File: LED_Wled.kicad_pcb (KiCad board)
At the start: 2 copper layers, 67 x 27 mm, 25 parts, among them J1 SWD_PORT_SKEDD, Q1 BSS138, Q2 AO4485, Q3 BSS138, Q4 AO4485, U1 ESP8266-12E_ESP-12E, U2 XL1509, U3 LD1117DT33TR

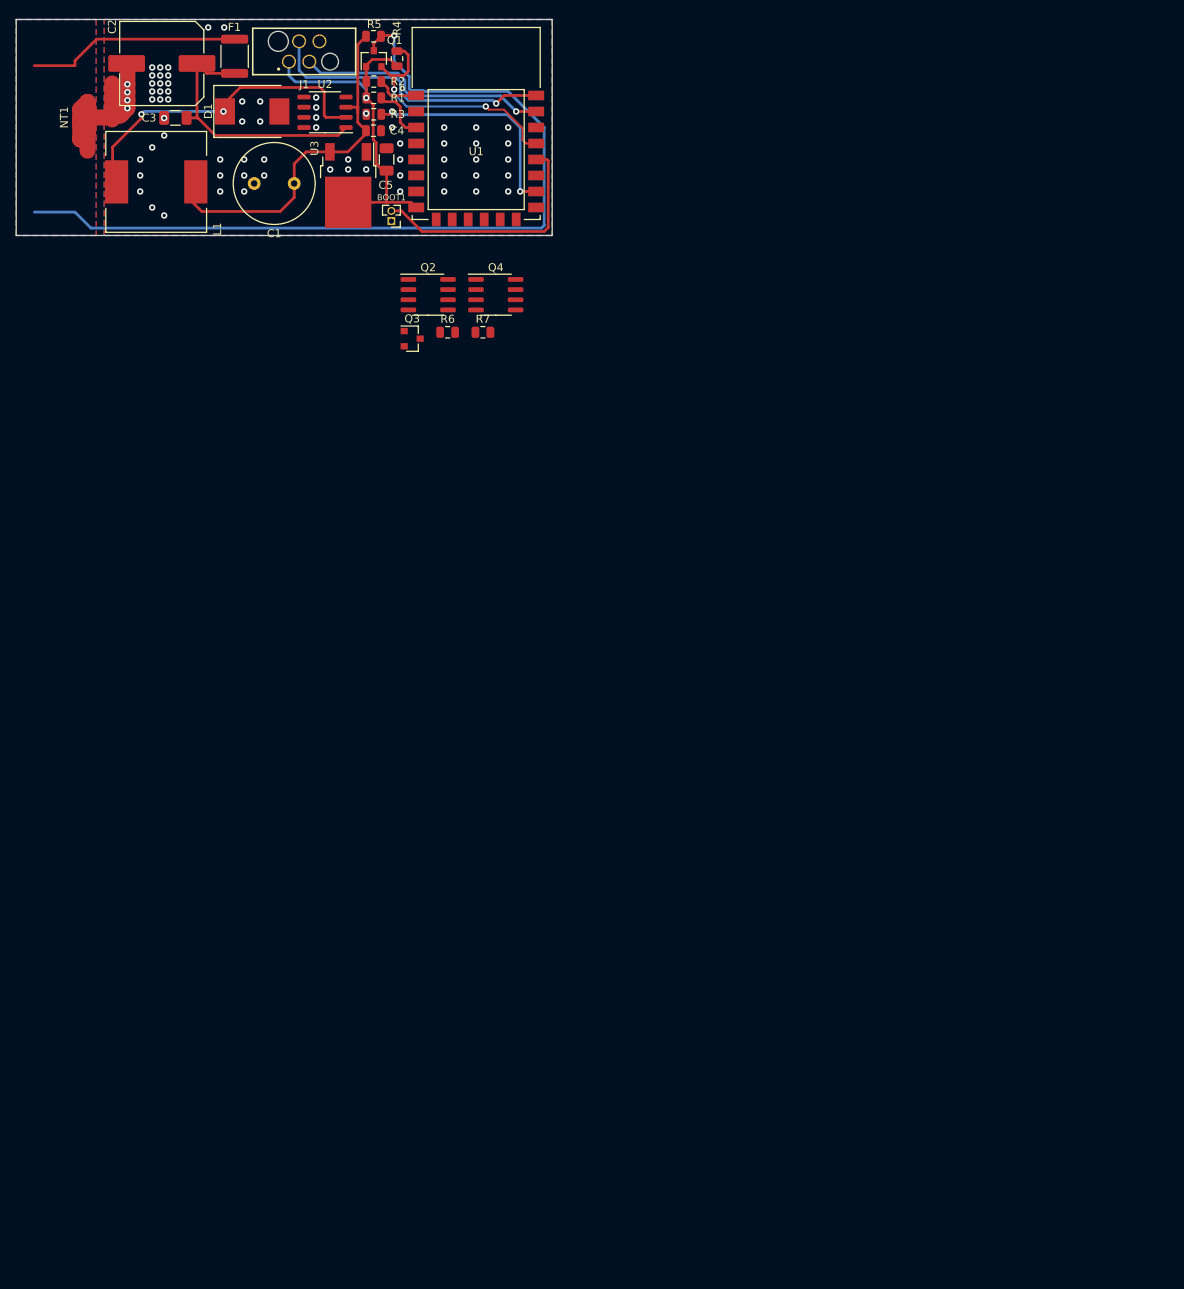
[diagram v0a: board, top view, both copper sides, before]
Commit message: pcb drawn, changed components
lm1117 to ams1117
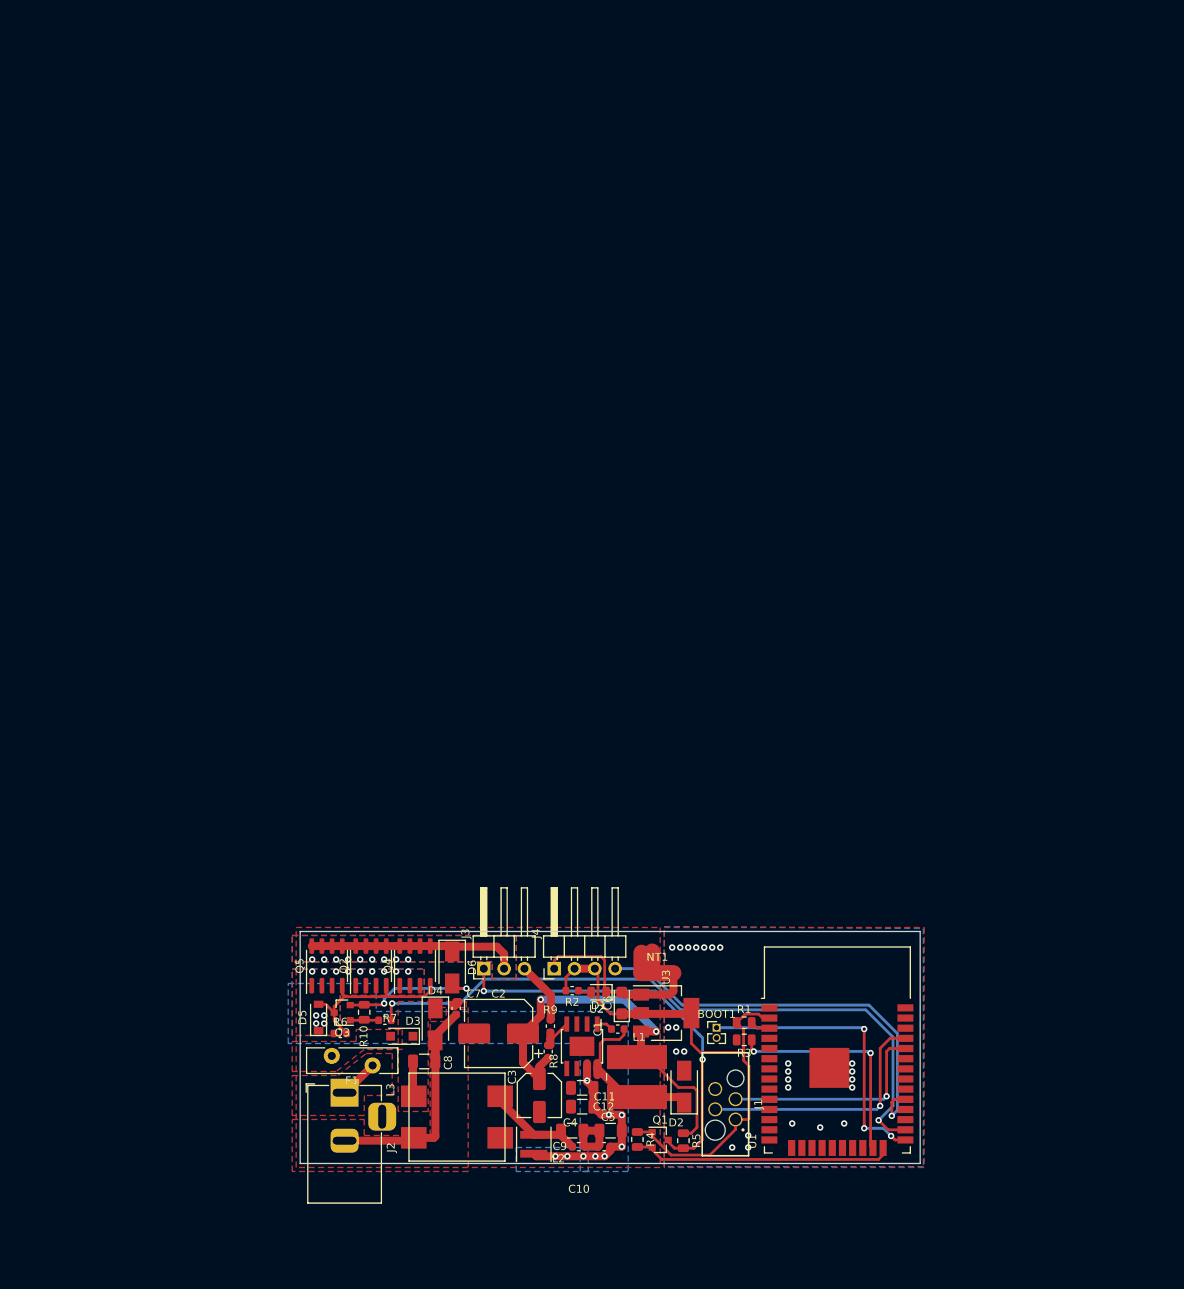
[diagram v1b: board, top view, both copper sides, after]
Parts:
- added C10: 0.1uF 50V, Capacitor_SMD:C_0603_1608Metric, F.Cu at (136.3, 186.9)
- added C11: 10uF 50V, Capacitor_SMD:C_1206_3216Metric, F.Cu at (140.3, 184.9)
- added C12: 0.1uF 50V, Capacitor_SMD:C_0603_1608Metric, F.Cu at (139.5, 186.9)
- added C6: 22uF 10V, Capacitor_Tantalum_SMD:CP_EIA-3216-10_Kemet-I, F.Cu at (141.7, 168.9)
- added C7: 0.1uF 50V, Capacitor_SMD:C_0603_1608Metric, F.Cu at (121.0, 169.6)
- added C8: 10uF 50V, Capacitor_SMD:C_1206_3216Metric, F.Cu at (117.0, 176.2)
- added C9: 10uF 50V, Capacitor_SMD:C_1206_3216Metric, F.Cu at (135.5, 184.9)
- added D2: SS34, Diode_SMD:D_SMA, F.Cu at (149.5, 179.4)
- added D3: SM4007, Diode_SMD:D_SOD-123F, F.Cu at (114.2, 173.1)
- added D4: SMAJ26CA, Diode_SMD:D_SMA, F.Cu at (118.4, 171.6)
- added D5: BZT52B15, Diode_SMD:D_SOD-123, F.Cu at (103.8, 170.8)
- added D6: SS34, Diode_SMD:D_SMA, F.Cu at (120.5, 164.5)
- added J2: Barrel_Jack, Connector_BarrelJack:BarrelJack_Horizontal, F.Cu at (107.0, 180.2)
- added J3: LED_pigtail JST-SM, Connector_PinHeader_2.54mm:PinHeader_1x03_P2.54mm_Horizontal, F.Cu at (124.5, 164.7)
- added J4: Conn_01x04, Connector_PinHeader_2.54mm:PinHeader_1x04_P2.54mm_Horizontal, F.Cu at (133.2, 164.7)
- added L2: 3.3 µH, 6.6 A, Inductor_SMD:L_Coilcraft_XxL4030, F.Cu at (130.7, 186.6)
- added L3: ACM1211, userdvc:ACM1211, F.Cu at (121.1, 183.2)
- added Q5: AO4485, Package_SO:SOIC-8_3.9x4.9mm_P1.27mm, F.Cu at (104.8, 164.3)
- added R10: 10k, Resistor_SMD:R_0805_2012Metric, F.Cu at (109.5, 170.1)
- added R8: 15k, Resistor_SMD:R_0603_1608Metric, F.Cu at (132.5, 175.0)
- added R9: 4.7k, Resistor_SMD:R_0603_1608Metric, F.Cu at (132.8, 171.8)
- C1: value 180uF/63V -> 10nF 50V; footprint Capacitor_THT:C_Radial_D10.0mm_H16.0mm_P5.00mm -> Capacitor_SMD:C_0603_1608Metric
- C2: value 470uF/35V -> 150 uF 16V; footprint Capacitor_SMD:C_Elec_10x10.2 -> Capacitor_SMD:CP_Elec_8x6.7
- C3: value 1uF/50V -> 22uF 16V; footprint Capacitor_SMD:C_1206_3216Metric -> Capacitor_SMD:C_Elec_5x5.4
- C4: value 100nF/50V -> 10uF 50V; footprint Capacitor_SMD:C_0805_2012Metric -> Capacitor_SMD:C_1206_3216Metric
- C5: value 10uF/50V -> 10uF 50V
- D1: value SS32 -> LED_Indicator_Red; footprint Diode_SMD:D_SMC -> LED_SMD:LED_0805_2012Metric
- F1: value Fuse_Small -> Polyfuse; footprint Fuse:Fuse_1812_4532Metric -> Fuse:Fuse_Bourns_MF-RG650
- L1: value 68uH -> 22uH/5A; footprint Inductor_SMD:L_12x12mm_H8mm -> Inductor_SMD:L_Wuerth_WE-PD2-Typ-L
- Q3: value BSS138 -> MMBT3904
- R2, R6: value 10k -> 4.7k; footprint Resistor_SMD:R_0805_2012Metric -> Resistor_SMD:R_0603_1608Metric
- R7: value 10k -> 1k; footprint Resistor_SMD:R_0805_2012Metric -> Resistor_SMD:R_0603_1608Metric
- U1: value ESP8266-12E_ESP-12E -> ESP32-WROOM-32; footprint LED_Wled:ESP-12E -> RF_Module:ESP32-WROOM-32
- U2: value XL1509 -> TPS5450DDAR; footprint Package_SO:SOP-8_3.9x4.9mm_P1.27mm -> Package_SO:TI_SO-PowerPAD-8
- U3: value LD1117DT33TR -> AMS1117-3.3; footprint Package_TO_SOT_SMD:TO-252-2 -> Package_TO_SOT_SMD:SOT-223-3_TabPin2
- moved R5 143.4 mm to (149.4, 186.2), turned to 270 degrees
- moved J1 141.7 mm to (154.7, 181.6), turned to 270 degrees
- moved Q1 139.8 mm to (146.5, 186.1), turned to 0 degrees
- moved R4 138.4 mm to (143.7, 186.0), turned to 270 degrees
- moved C3 130.4 mm to (131.4, 180.5), turned to 270 degrees
- moved C2 128.4 mm to (126.3, 172.8)
- moved NT1 127.9 mm to (146.2, 165.2)
- moved L1 127.0 mm to (143.6, 178.2), turned to 90 degrees
- moved F1 125.5 mm to (105.5, 175.6), turned to 0 degrees
- moved C4 124.8 mm to (136.8, 181.9)
- moved R3 124.6 mm to (157.0, 173.6)
- moved R1 124.5 mm to (157.0, 171.4)
- moved U1 123.8 mm to (168.7, 177.8)
- moved U2 121.1 mm to (136.7, 174.4), turned to 270 degrees
- moved C5 118.6 mm to (136.8, 179.6), turned to 0 degrees
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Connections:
- net LED_OUT_HV renamed LED_OUT_HS1
- BOOT1 pad 1: GND -> Net-(BOOT1-Pad1)
- BOOT1 pad 2: Net-(BOOT1-Pad2) -> GND
- C1 pad 1: +5V -> Net-(C1-Pad1)
- C1 pad 2: GND -> Net-(C1-Pad2)
- C2 pad 1: Net-(C2-Pad1) -> +5V
- C2 pad 2: GND -> GNDPWR
- C3 pad 1: Net-(C2-Pad1) -> +5V
- C3 pad 2: GND -> GNDPWR
- C4 pad 1: +5V -> GNDPWR
- C4 pad 2: GND -> Vin
- C5 pad 1: +3V3 -> GNDPWR
- C5 pad 2: GND -> Vin
- D1 pad 1: Net-(D1-Pad1) -> GND
- D1 pad 2: GND -> Net-(D1-Pad2)
- F1 pad 1: VIN -> Net-(D3-Pad2)
- F1 pad 2: Net-(C2-Pad1) -> VBat+
- L1 pad 1: Net-(D1-Pad1) -> Net-(C1-Pad1)
- Q1 pad 2: LED_OUT_LV -> LED_OUT_LS1
- Q2 pad 1: LED_VOUT -> Vin
- Q2 pad 2: Net-(Q2-Pad2) -> Vin
- Q2 pad 3: LED_VOUT -> Vin
- Q2 pad 4: Net-(Q2-Pad2) -> Net-(D5-Pad2)
- Q2 pad 5: VIN -> LED_VOUT
- Q2 pad 6: VIN -> LED_VOUT
- Q2 pad 7: VIN -> LED_VOUT
- Q2 pad 8: VIN -> LED_VOUT
- Q3 pad 1: +3V3 -> Net-(Q3-Pad1)
- Q3 pad 2: LED_VOUT_sw -> Net-(D6-Pad2)
- Q3 pad 3: Net-(Q2-Pad2) -> Net-(D5-Pad2)
- Q4 pad 1: LED_VOUT -> Vin
- Q4 pad 2: Net-(Q2-Pad2) -> Vin
- Q4 pad 3: (no net) -> Vin
- Q4 pad 4: (no net) -> Net-(D5-Pad2)
- Q4 pad 5: (no net) -> LED_VOUT
- Q4 pad 6: (no net) -> LED_VOUT
- Q4 pad 7: VIN -> LED_VOUT
- Q4 pad 8: VIN -> LED_VOUT
- R2 pad 1: Net-(R2-Pad1) -> Net-(D1-Pad2)
- R4 pad 2: LED_OUT_LV -> LED_OUT_LS1
- R6 pad 1: +3V3 -> Vin
- R6 pad 2: LED_VOUT_sw -> Net-(D5-Pad2)
- R7 pad 1: +5V -> Net-(Q3-Pad1)
- R7 pad 2: Net-(Q2-Pad2) -> LED_VOUT_LS1
- U1 pad 1: Net-(R2-Pad1) -> GND
- U1 pad 16: Net-(R3-Pad1) -> (no net)
- U1 pad 18: Net-(BOOT1-Pad2) -> (no net)
- U1 pad 19: LED_OUT_LV -> (no net)
- U1 pad 2: (no net) -> +3V3
- U1 pad 21: RXD -> (no net)
- U1 pad 22: TXD -> (no net)
- U1 pad 8: +3V3 -> (no net)
- U2 pad 1: Net-(C2-Pad1) -> Net-(C1-Pad2)
- U2 pad 2: Net-(D1-Pad1) -> (no net)
- U2 pad 3: +5V -> (no net)
- U2 pad 4: (no net) -> Net-(R8-Pad2)
- U2 pad 5: GND -> (no net)
- U2 pad 6: GND -> GNDPWR
- U2 pad 7: GND -> Vin
- U2 pad 8: GND -> Net-(C1-Pad1)
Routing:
- net LED_VOUT_LS1: track 0.00 -> 84.0 mm, vias 0 -> 2
- net LED_OUT_HS1: track 107.1 -> 50.9 mm, vias 1 -> 2
- net MIC: track 0.00 -> 52.8 mm, vias 0 -> 1
- net Net-(D1-Pad1): track 40.2 -> 0.00 mm, vias 2 -> 0
- net Net-(BOOT1-Pad1): track 0.00 -> 36.7 mm, vias 0 -> 3
- net Net-(C2-Pad1): track 33.3 -> 0.00 mm
- net LED_OUT_LS1: track 0.00 -> 32.6 mm
- net LED_OUT_LV: track 31.4 -> 0.00 mm, vias 2 -> 0
- net Net-(BOOT1-Pad2): track 30.8 -> 0.00 mm
- net VBat-: track 0.00 -> 30.8 mm
- net LED_VOUT: track 0.00 -> 26.8 mm, vias 0 -> 9
- net VIN: track 26.8 -> 0.00 mm
- net Vin: track 0.00 -> 25.6 mm, vias 0 -> 22
- net +3V3: track 44.9 -> 68.5 mm, vias 1 -> 0
- net Net-(D5-Pad2): track 0.00 -> 22.7 mm
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- added copper zone on F.Cu, net /PWR_Line
- added copper zone on B.Cu, net LED_VOUT
- added copper zone on F.Cu, net LED_VOUT
- added copper zone on F.Cu, net Net-(D3-Pad2)
- added copper zone on F.Cu, net VBat+
- added copper zone on F.Cu, net VBat-
- added copper zone on B.Cu, net Vin
- added copper zone on F.Cu, net Vin
- removed copper zone on B.Cu, net VIN
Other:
- board size 67 x 27 mm -> 77.5 x 29 mm
- board text removed: "D_OUT"
- board text removed: "For use with ARGB LED-strip MAX INPUT: +30 V"
- board text removed: "GNDPWR"
- board text removed: "VIN"
- board text removed: "remote-led-project 2022-01-13 rev1.1"

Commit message: test
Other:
- board text added: "test"

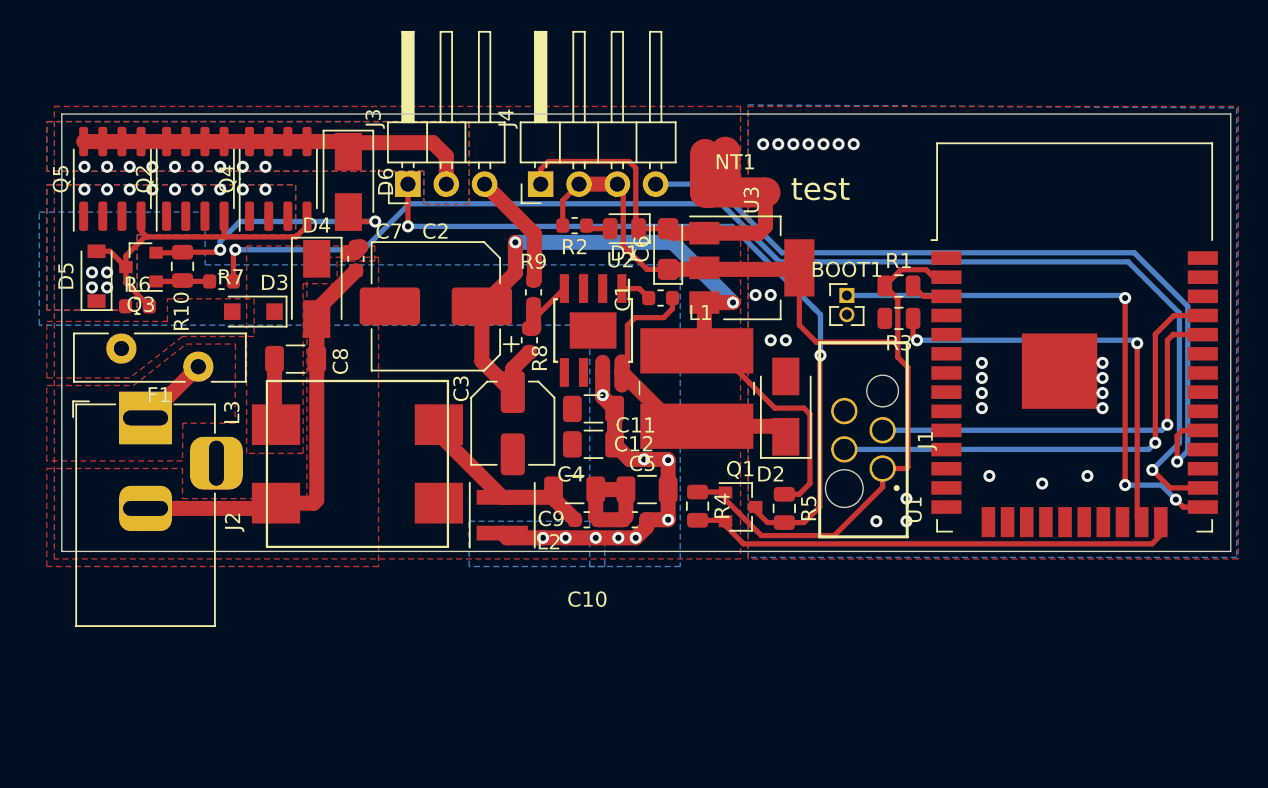
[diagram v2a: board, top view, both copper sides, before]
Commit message: connector changes, pcb redesign
added +5V output with switch with mosfet, changed level shifter from transistor to buffer 4chan, added 2 more led strip channels
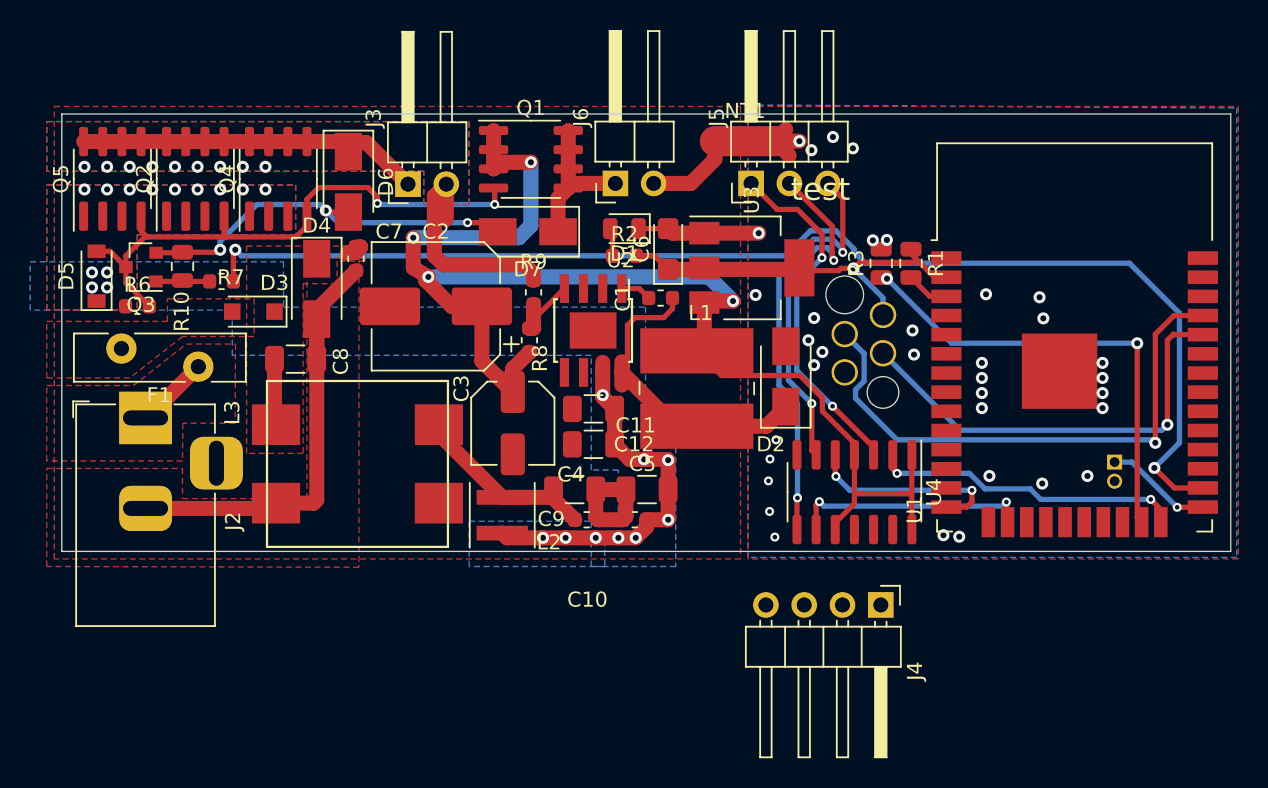
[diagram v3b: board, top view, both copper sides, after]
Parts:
- removed R4, R5: 10k, Resistor_SMD:R_0805_2012Metric
- added D7: SS34, Diode_SMD:D_SMA, F.Cu at (132.4, 167.8)
- added J5: LED_signal_chan, Connector_PinHeader_2.54mm:PinHeader_1x03_P2.54mm_Horizontal, F.Cu at (147.2, 164.6)
- added J6: +5V Out, Connector_PinHeader_2.54mm:PinHeader_1x02_P2.54mm_Horizontal, F.Cu at (138.2, 164.6)
- added U4: SN74HC125DR, Package_SO:SOIC-14_3.9x8.7mm_P1.27mm, F.Cu at (154.1, 185.1)
- BOOT1, J1: moved to B.Cu
- J3: value LED_pigtail JST-SM -> VIN-Out; footprint Connector_PinHeader_2.54mm:PinHeader_1x03_P2.54mm_Horizontal -> Connector_PinHeader_2.54mm:PinHeader_1x02_P2.54mm_Horizontal
- J4: value Conn_01x04 -> Microphone input
- Q1: value BSS138 -> AO4485; footprint Package_TO_SOT_SMD:SOT-23 -> Package_SO:SOIC-8_3.9x4.9mm_P1.27mm
- moved J4 35.9 mm to (155.8, 192.6), turned to 270 degrees
- moved Q1 26.9 mm to (132.6, 163.0)
- moved BOOT1 20.9 mm to (171.3, 183.1), turned to 180 degrees
- moved J1 6.38 mm to (154.7, 175.2), turned to 90 degrees
- moved R2 3.86 mm to (138.8, 169.4), turned to 0 degrees
- moved R3 3.83 mm to (155.8, 169.9), turned to 90 degrees
- moved NT1 3.46 mm to (146.8, 161.8)
- moved D2 2.00 mm to (149.5, 177.4)
- moved R1 1.70 mm to (157.8, 169.9), turned to 270 degrees
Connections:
- net LED_VOUT_LS1 renamed LED_VOUT_SWS
- J3 pad 1: LED_OUT_HS1 -> LED_VOUT
- J3 pad 2: LED_VOUT -> GNDPWR
- Q1 pad 1: +3V3 -> +5V
- Q1 pad 2: LED_OUT_LS1 -> +5V
- Q1 pad 3: LED_OUT_HS1 -> +5V
- U1 pad 14: (no net) -> LED_OUT_LS2
- U1 pad 16: (no net) -> LED_OUT_LS3
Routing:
- net MIC: track 52.8 -> 0.00 mm, vias 1 -> 0
- net +3V3: track 68.5 -> 26.9 mm, vias 0 -> 1
- net +5V: track 52.0 -> 89.9 mm, vias 2 -> 4
- net Net-(BOOT1-Pad1): track 36.7 -> 7.10 mm, vias 3 -> 1
- net LED_OUT_HS3: track 0.00 -> 28.1 mm, vias 0 -> 2
- net LED_OUT_HS1: track 50.9 -> 23.5 mm
- net LED_OUT_HS2: track 0.00 -> 23.3 mm, vias 0 -> 2
- net LED_OUT_LS3: track 0.00 -> 15.9 mm, vias 0 -> 2
- net Net-(D5-Pad2): track 22.7 -> 38.4 mm, vias 0 -> 2
- net LED_OUT_LS2: track 0.00 -> 13.5 mm, vias 0 -> 2
- net LED_OUT_LS1: track 32.6 -> 20.7 mm, vias 0 -> 2
- net LED_5VOUT: track 0.00 -> 10.2 mm
- net GND: track 22.8 -> 12.6 mm, vias 25 -> 35
- net Net-(D6-Pad2): track 17.6 -> 26.4 mm, vias 2 -> 3
- net GNDPWR: track 21.6 -> 28.6 mm
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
